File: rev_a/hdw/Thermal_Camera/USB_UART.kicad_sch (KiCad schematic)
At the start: 22 parts

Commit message: lots of schematic progress
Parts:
- C? (x6): footprint Capacitors_SMD:C_0603 -> (none); Digi-Key PN 1276-1935-1-ND -> (none); display_footprint 0603 -> (none)
- C? (x3): footprint Capacitors_SMD:C_0603 -> (none); Digi-Key PN 1276-1871-1-ND -> (none); display_footprint 0603 -> (none)
- C? (x2): footprint Capacitors_SMD:C_0603 -> (none); Digi-Key PN 13-CC0603JPNPO9BN470CT-ND -> (none); display_footprint 0603 -> (none)
- D?: footprint LEDs:LED_0603 -> (none); Digi-Key PN 754-1124-1-ND -> (none)
- R?: footprint Resistors_SMD:R_0603 -> (none); Digi-Key PN 541-10.0KHCT-ND -> (none); Wattage 1/10W -> (none); display_footprint 0603 -> (none)
- R? (x2): footprint Resistors_SMD:R_0603 -> (none); Wattage 1/10W -> (none); display_footprint 0603 -> (none)
- R? (x2): footprint Resistors_SMD:R_0603 -> (none); Digi-Key PN 541-5306-1-ND -> (none); Wattage 1/10W -> (none); display_footprint 0603 -> (none)
- R?: footprint Resistors_SMD:R_0603 -> (none); Digi-Key PN 541-1.00KHCT-ND -> (none); Wattage 1/10W -> (none); display_footprint 0603 -> (none)
- gave numbers to parts that had none: 2

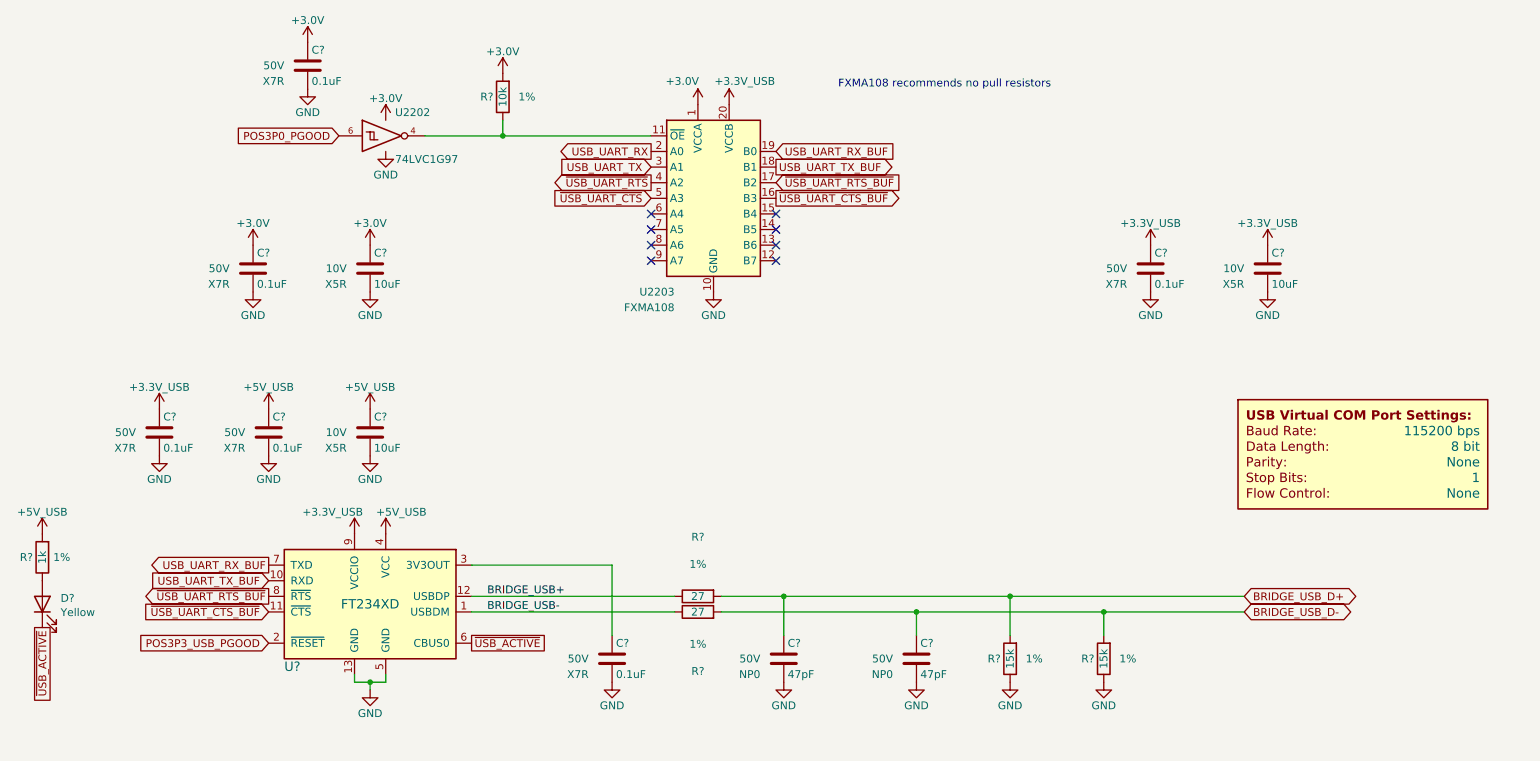
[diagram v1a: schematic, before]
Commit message: assigned a ton of footprints
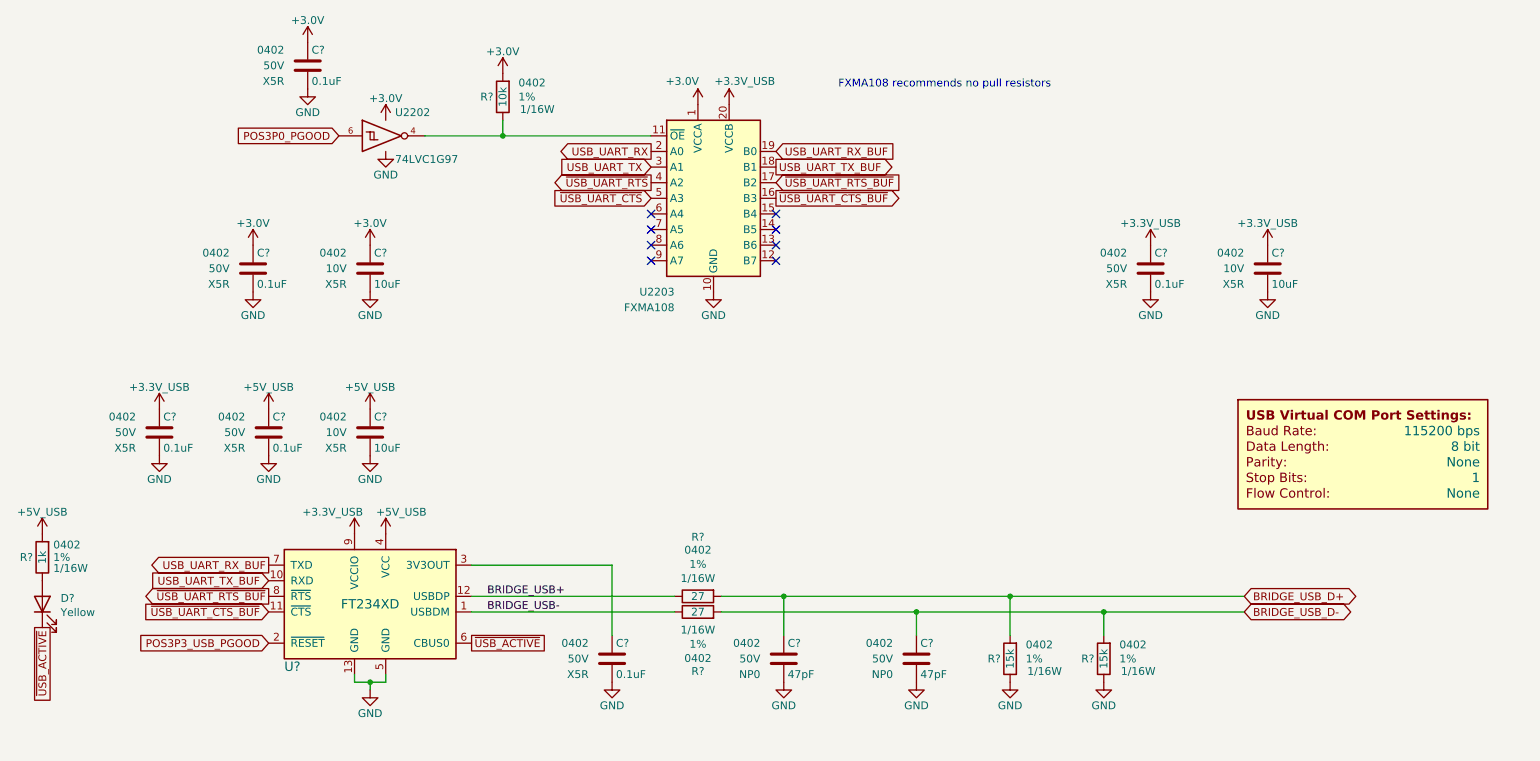
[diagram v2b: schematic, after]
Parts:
- C? (x6): footprint (none) -> Capacitors_SMD:C_0402; Dielectric X7R -> X5R; display_footprint (none) -> 0402
- C? (x5): footprint (none) -> Capacitors_SMD:C_0402; display_footprint (none) -> 0402
- D?: footprint (none) -> LEDs:LED_0402
- R? (x6): footprint (none) -> Resistors_SMD:R_0402; Wattage (none) -> 1/16W; display_footprint (none) -> 0402
- U2202: Digi-Key PN (none) -> 296-15582-1-ND
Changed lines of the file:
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@@
 			)
 		)
-		(property "Footprint" ""
+		(property "Footprint" "Resistors_SMD:R_0402"
 			(at 100.33 29.21 0)
 			(effects
@@
 			)
 		)
-		(property "display_footprint" ""
+		(property "display_footprint" "0402"
 			(at 102.87 26.924 0)
 			(effects
@@
 			)
 		)
-		(property "Wattage" ""
+		(property "Wattage" "1/16W"
 			(at 103.124 31.242 0)
 			(effects
@@
 			)
 		)
-		(property "Footprint" ""
+		(property "Footprint" "Resistors_SMD:R_0402"
 			(at 198.12 120.65 0)
 			(effects
@@
 			)
 		)
-		(property "display_footprint" ""
+		(property "display_footprint" "0402"
 			(at 200.66 118.364 0)
 			(effects
@@
 			)
 		)
-		(property "Wattage" ""
+		(property "Wattage" "1/16W"
 			(at 200.914 122.682 0)
 			(effects
@@
 			)
 		)
-		(property "Footprint" ""
+		(property "Footprint" "Capacitors_SMD:C_0402"
 			(at 60.6552 60.96 0)
 			(effects
@@
 			)
 		)
-		(property "display_footprint" ""
+		(property "display_footprint" "0402"
 			(at 55.88 54.61 0)
 			(effects
@@
 			)
 		)
-		(property "Dielectric" "X7R"
+		(property "Dielectric" "X5R"
 			(at 55.88 59.69 0)
 			(effects
@@
 			)
 		)
-		(property "Footprint" ""
+		(property "Footprint" "Capacitors_SMD:C_0402"
 			(at 45.4152 87.63 0)
 			(effects
@@
 			)
 		)
-		(property "display_footprint" ""
+		(property "display_footprint" "0402"
 			(at 40.64 81.28 0)
 			(effects
@@
 			)
 		)
-		(property "Dielectric" "X7R"
+		(property "Dielectric" "X5R"
 			(at 40.64 86.36 0)
 			(effects
@@
 			)
 		)
-		(property "Footprint" ""
+		(property "Footprint" "Resistors_SMD:R_0402"
 			(at 132.08 110.49 0)
 			(effects
@@
 			)
 		)
-		(property "display_footprint" ""
+		(property "display_footprint" "0402"
 			(at 132.08 102.9462 90)
 			(effects
@@
 			)
 		)
-		(property "Wattage" ""
+		(property "Wattage" "1/16W"
 			(at 132.08 107.569 90)
 			(effects
@@
 			)
 		)
+		(property "Digi-Key PN" "296-15582-1-ND"
+			(at 81.28 35.56 0)
+			(effects
+				(font
+					(size 1.27 1.27)
+				)
+				(hide yes)
+			)
+		)
 		(pin "1"
 		)
@@
 			)
 		)
-		(property "Footprint" ""
+		(property "Footprint" "Resistors_SMD:R_0402"
 			(at 182.88 120.65 0)
 			(effects
@@
 			)
 		)
-		(property "display_footprint" ""
+		(property "display_footprint" "0402"
 			(at 185.42 118.364 0)
 			(effects
@@
 			)
 		)
-		(property "Wattage" ""
+		(property "Wattage" "1/16W"
 			(at 185.674 122.682 0)
 			(effects
@@
 			)
 		)
-		(property "Footprint" ""
+		(property "Footprint" "Resistors_SMD:R_0402"
 			(at 25.4 104.14 0)
 			(effects
@@
 			)
 		)
-		(property "display_footprint" ""
+		(property "display_footprint" "0402"
 			(at 27.178 102.108 0)
 			(effects
@@
 			)
 		)
-		(property "Wattage" ""
+		(property "Wattage" "1/16W"
 			(at 27.178 105.918 0)
 			(effects
@@
 			)
 		)
-		(property "Footprint" ""
+		(property "Footprint" "Capacitors_SMD:C_0402"
 			(at 79.7052 87.63 0)
 			(effects
@@
 			)
 		)
-		(property "display_footprint" ""
+		(property "display_footprint" "0402"
 			(at 74.93 81.28 0)
 			(effects
@@
 			)
 		)
-		(property "Footprint" ""
+		(property "Footprint" "Capacitors_SMD:C_0402"
 			(at 168.6052 124.46 0)
 			(effects
@@
 			)
 		)
-		(property "display_footprint" ""
+		(property "display_footprint" "0402"
 			(at 163.83 118.11 0)
 			(effects
@@
 			)
 		)
-		(property "Footprint" ""
+		(property "Footprint" "Capacitors_SMD:C_0402"
 			(at 147.0152 124.46 0)
 			(effects
@@
 			)
 		)
-		(property "display_footprint" ""
+		(property "display_footprint" "0402"
 			(at 142.24 118.11 0)
 			(effects
@@
 			)
 		)
-		(property "Footprint" ""
+		(property "Footprint" "Capacitors_SMD:C_0402"
 			(at 63.1952 87.63 0)
 			(effects
@@
 			)
 		)
-		(property "display_footprint" ""
+		(property "display_footprint" "0402"
 			(at 58.42 81.28 0)
 			(effects
@@
 			)
 		)
-		(property "Dielectric" "X7R"
+		(property "Dielectric" "X5R"
 			(at 58.42 86.36 0)
 			(effects
@@
 			)
 		)
-		(property "Footprint" ""
+		(property "Footprint" "Resistors_SMD:R_0402"
 			(at 132.08 113.03 0)
 			(effects
@@
 			)
 		)
-		(property "display_footprint" ""
+		(property "display_footprint" "0402"
 			(at 132.08 120.5738 90)
 			(effects
@@
 			)
 		)
-		(property "Wattage" ""
+		(property "Wattage" "1/16W"
 			(at 132.08 115.951 90)
 			(effects
@@
 			)
 		)
-		(property "Footprint" ""
+		(property "Footprint" "Capacitors_SMD:C_0402"
 			(at 206.7052 60.96 0)
 			(effects
@@
 			)
 		)
-		(property "display_footprint" ""
+		(property "display_footprint" "0402"
 			(at 201.93 54.61 0)
 			(effects
@@
 			)
 		)
-		(property "Dielectric" "X7R"
+		(property "Dielectric" "X5R"
 			(at 201.93 59.69 0)
 			(effects
@@
 			)
 		)
-		(property "Footprint" ""
+		(property "Footprint" "Capacitors_SMD:C_0402"
 			(at 225.7552 60.96 0)
 			(effects
@@
 			)
 		)
-		(property "display_footprint" ""
+		(property "display_footprint" "0402"
 			(at 220.98 54.61 0)
 			(effects
@@
 			)
 		)
-		(property "Footprint" ""
+		(property "Footprint" "Capacitors_SMD:C_0402"
 			(at 79.7052 60.96 0)
 			(effects
@@
 			)
 		)
-		(property "display_footprint" ""
+		(property "display_footprint" "0402"
 			(at 74.93 54.61 0)
 			(effects
@@
 			)
 		)
-		(property "Footprint" ""
+		(property "Footprint" "Capacitors_SMD:C_0402"
 			(at 69.5452 27.94 0)
 			(effects
@@
 			)
 		)
-		(property "display_footprint" ""
+		(property "display_footprint" "0402"
 			(at 64.77 21.59 0)
 			(effects
@@
 			)
 		)
-		(property "Dielectric" "X7R"
+		(property "Dielectric" "X5R"
 			(at 64.77 26.67 0)
 			(effects
@@
 			)
 		)
-		(property "Footprint" ""
+		(property "Footprint" "LEDs:LED_0402"
 			(at 25.4 111.76 0)
 			(effects
@@
 			)
 		)
-		(property "Footprint" ""
+		(property "Footprint" "Capacitors_SMD:C_0402"
 			(at 119.0752 124.46 0)
 			(effects
@@
 			)
 		)
-		(property "display_footprint" ""
+		(property "display_footprint" "0402"
 			(at 114.3 118.11 0)
 			(effects
@@
 			)
 		)
-		(property "Dielectric" "X7R"
+		(property "Dielectric" "X5R"
 			(at 114.3 123.19 0)
 			(effects

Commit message: assigned some part numbers
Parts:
- C? (x6): Digi-Key PN (none) -> 490-10697-1-ND
- C? (x3): Digi-Key PN (none) -> 490-GRM155R61A106ME11DCT-ND
- C? (x2): Digi-Key PN (none) -> 490-5942-1-ND
- D?: Digi-Key PN (none) -> VLMY1500-GS08CT-ND
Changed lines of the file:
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@@
 			)
 		)
-		(property "Digi-Key PN" ""
+		(property "Digi-Key PN" "490-10697-1-ND"
 			(at 70.485 44.45 0)
 			(effects
@@
 			)
 		)
-		(property "Digi-Key PN" ""
+		(property "Digi-Key PN" "490-10697-1-ND"
 			(at 55.245 71.12 0)
 			(effects
@@
 			)
 		)
-		(property "Digi-Key PN" ""
+		(property "Digi-Key PN" "490-GRM155R61A106ME11DCT-ND"
 			(at 78.74 83.82 0)
 			(effects
@@
 			)
 		)
-		(property "Digi-Key PN" ""
+		(property "Digi-Key PN" "490-5942-1-ND"
 			(at 167.64 120.65 0)
 			(effects
@@
 			)
 		)
-		(property "Digi-Key PN" ""
+		(property "Digi-Key PN" "490-5942-1-ND"
 			(at 146.05 120.65 0)
 			(effects
@@
 			)
 		)
-		(property "Digi-Key PN" ""
+		(property "Digi-Key PN" "490-10697-1-ND"
 			(at 73.025 71.12 0)
 			(effects
@@
 			)
 		)
-		(property "Digi-Key PN" ""
+		(property "Digi-Key PN" "490-10697-1-ND"
 			(at 216.535 44.45 0)
 			(effects
@@
 			)
 		)
-		(property "Digi-Key PN" ""
+		(property "Digi-Key PN" "490-GRM155R61A106ME11DCT-ND"
 			(at 224.79 57.15 0)
 			(effects
@@
 			)
 		)
-		(property "Digi-Key PN" ""
+		(property "Digi-Key PN" "490-GRM155R61A106ME11DCT-ND"
 			(at 78.74 57.15 0)
 			(effects
@@
 			)
 		)
-		(property "Digi-Key PN" ""
+		(property "Digi-Key PN" "490-10697-1-ND"
 			(at 79.375 11.43 0)
 			(effects
@@
 			)
 		)
-		(property "Digi-Key PN" ""
+		(property "Digi-Key PN" "VLMY1500-GS08CT-ND"
 			(at 155.448 280.416 0)
 			(effects
@@
 			)
 		)
-		(property "Digi-Key PN" ""
+		(property "Digi-Key PN" "490-10697-1-ND"
 			(at 128.905 107.95 0)
 			(effects

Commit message: assigned resistor part numbers
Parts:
- R?: Digi-Key PN (none) -> RMCF0402FT10K0CT-ND
- R? (x2): Digi-Key PN (none) -> RMCF0402FT15K0CT-ND
- R? (x2): Digi-Key PN (none) -> RMCF0402FT27R0CT-ND
- R?: Digi-Key PN (none) -> RMCF0402FT1K00CT-ND
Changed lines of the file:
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@@
 			)
 		)
-		(property "Digi-Key PN" ""
+		(property "Digi-Key PN" "RMCF0402FT10K0CT-ND"
 			(at 107.95 19.05 0)
 			(effects
@@
 			)
 		)
-		(property "Digi-Key PN" ""
+		(property "Digi-Key PN" "RMCF0402FT15K0CT-ND"
 			(at 205.74 110.49 0)
 			(effects
@@
 			)
 		)
-		(property "Digi-Key PN" ""
+		(property "Digi-Key PN" "RMCF0402FT27R0CT-ND"
 			(at 142.24 102.87 0)
 			(effects
@@
 			)
 		)
-		(property "Digi-Key PN" ""
+		(property "Digi-Key PN" "RMCF0402FT15K0CT-ND"
 			(at 190.5 110.49 0)
 			(effects
@@
 			)
 		)
-		(property "Digi-Key PN" ""
+		(property "Digi-Key PN" "RMCF0402FT1K00CT-ND"
 			(at 33.02 93.98 0)
 			(effects
@@
 			)
 		)
-		(property "Digi-Key PN" ""
+		(property "Digi-Key PN" "RMCF0402FT27R0CT-ND"
 			(at 142.24 120.65 0)
 			(effects
